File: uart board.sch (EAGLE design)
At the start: 15 parts, among them IC2 74LS688N, IC3 74LS590N

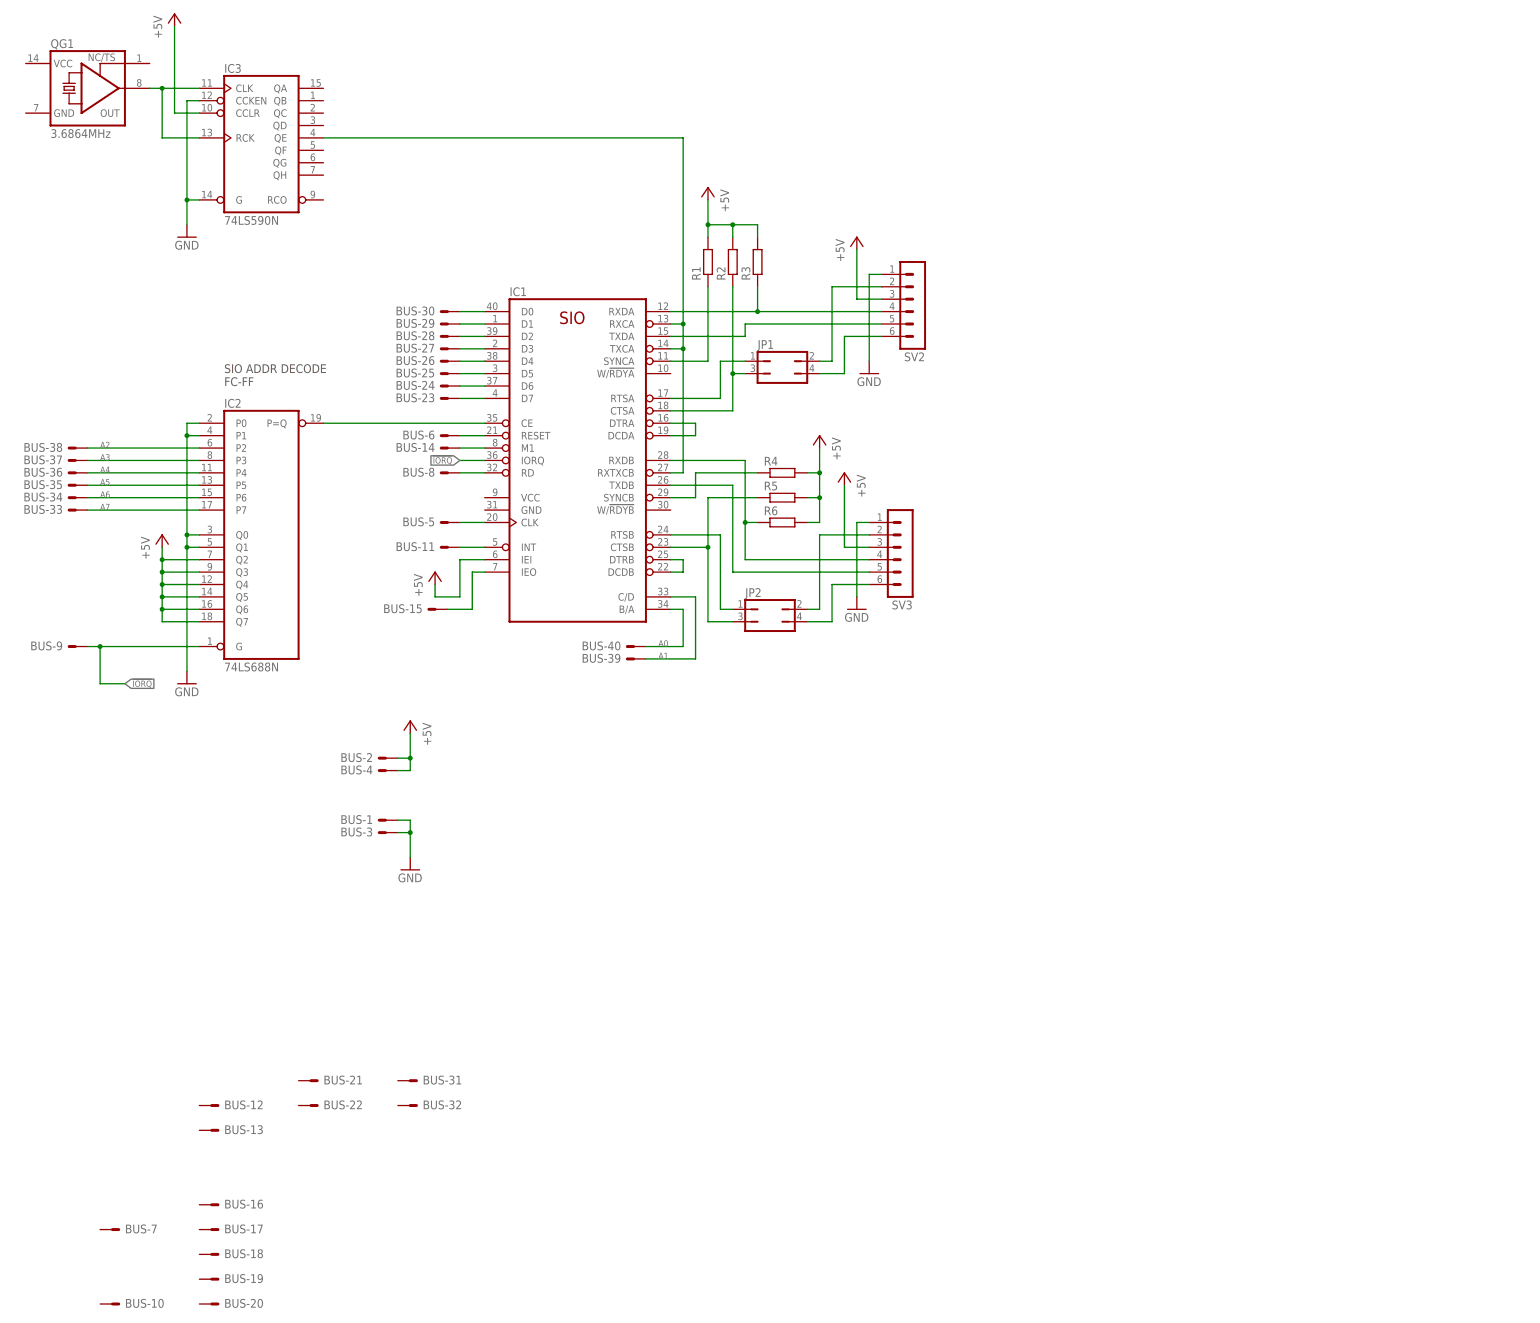
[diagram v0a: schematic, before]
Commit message: Interrupt daisy chain modification
To overcome the issue identified earlier, it seems better to change the interrupt daisy chain to make the CTC the higher priority device. This also simplifies the extra required circuitry to only a single OR gate (U13A).

Now, only when the IEO/ signal of the CTC is asserted will the board drive the data bus to the CPU.

Also added in a previous revision is changes to the beeper circuit. Will now be driven by a 555 timer, gated by the output register.
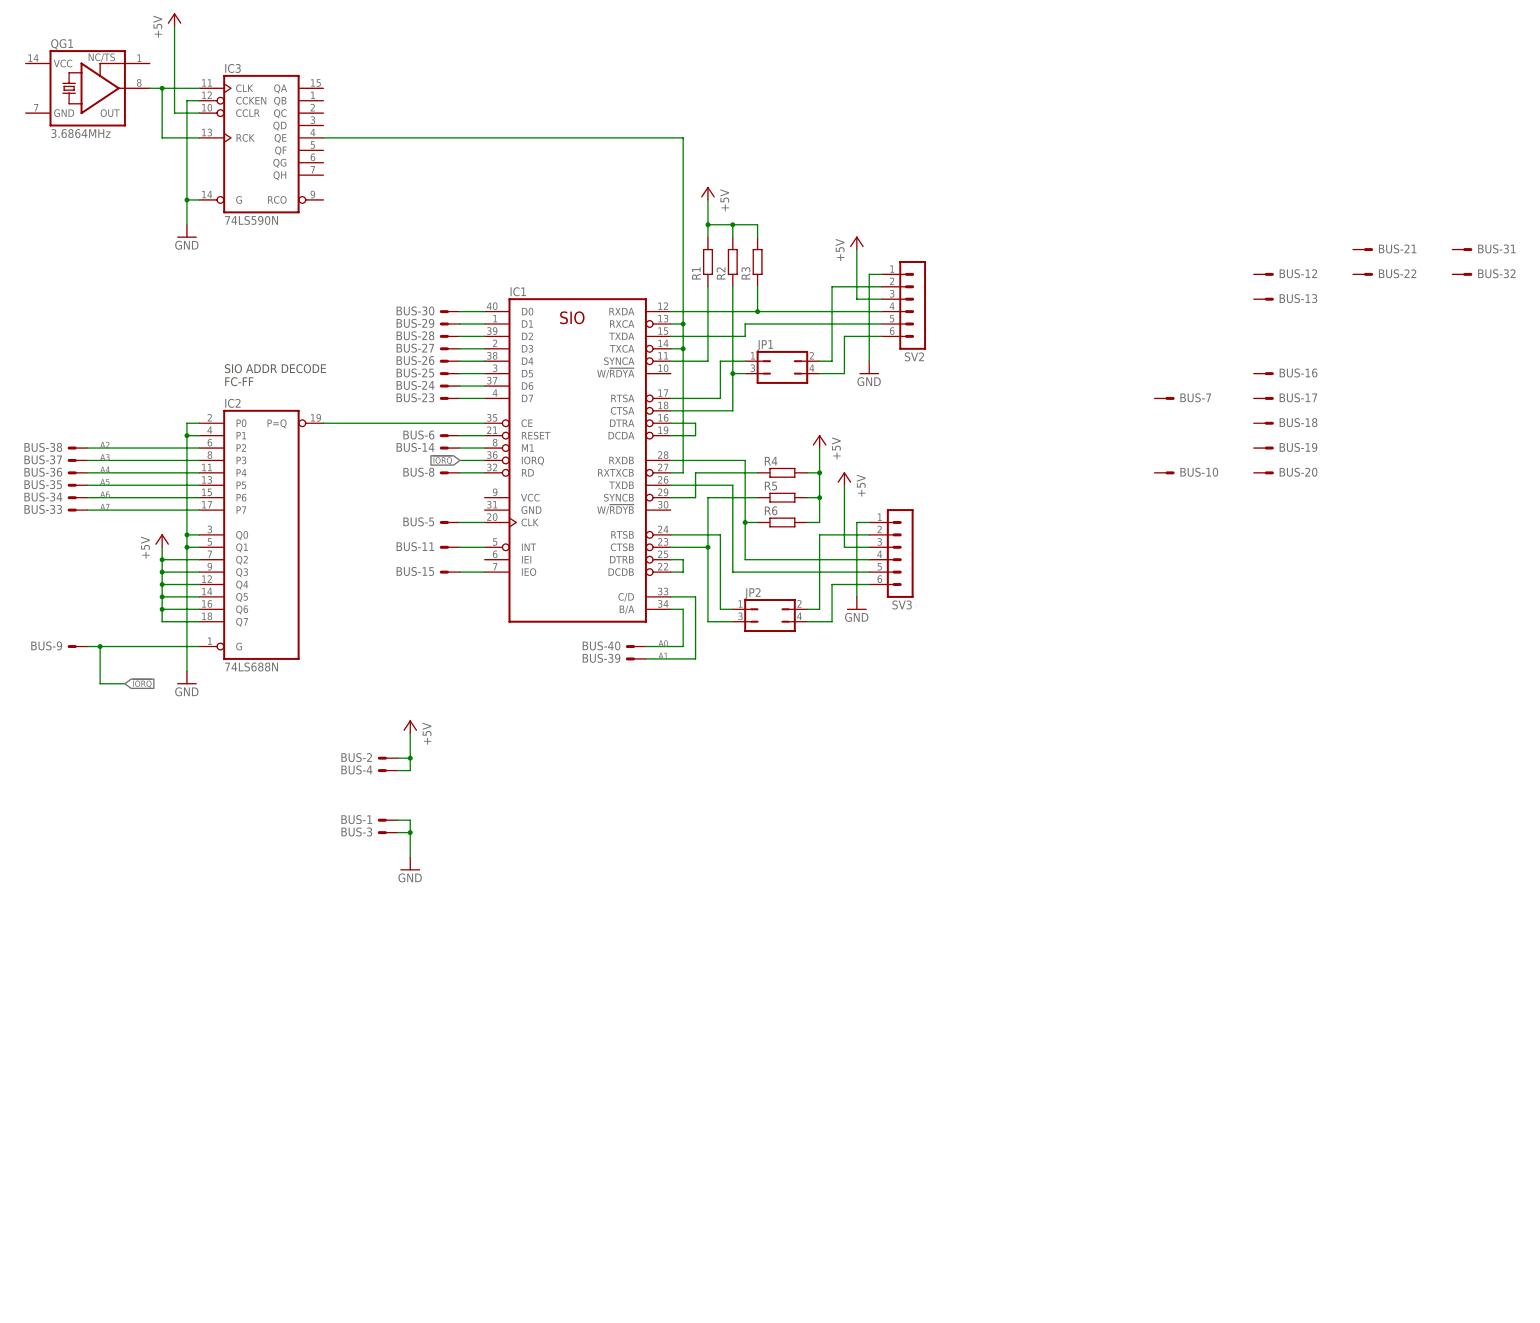
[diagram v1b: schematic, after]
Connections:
- net +5V: no longer IC1.IEI
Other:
- moved on the sheet: BUS-10, BUS-12, BUS-13, BUS-15, BUS-16, BUS-17, BUS-18, BUS-19, BUS-20, BUS-21, BUS-22, BUS-31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
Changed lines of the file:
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@@
 <part name="P+7" library="supply1" deviceset="+5V" device=""/>
 <part name="GND5" library="supply1" deviceset="GND" device=""/>
-<part name="P+8" library="supply1" deviceset="+5V" device=""/>
 </parts>
 <sheets>
@@
 <attribute name="VALUE" x="109.474" y="93.599" size="1.778" layer="96" rot="MR0"/>
 </instance>
-<instance part="BUS" gate="-7" x="40.64" y="-66.04" smashed="yes">
-<attribute name="NAME" x="43.18" y="-66.802" size="1.778" layer="95"/>
-<attribute name="VALUE" x="40.386" y="-68.961" size="1.778" layer="96"/>
+<instance part="BUS" gate="-7" x="256.54" y="104.14" smashed="yes">
+<attribute name="NAME" x="259.08" y="103.378" size="1.778" layer="95"/>
+<attribute name="VALUE" x="256.286" y="101.219" size="1.778" layer="96"/>
 </instance>
 <instance part="BUS" gate="-8" x="109.22" y="88.9" smashed="yes" rot="MR0">
@@
 <attribute name="VALUE" x="33.274" y="50.419" size="1.778" layer="96" rot="MR0"/>
 </instance>
-<instance part="BUS" gate="-10" x="40.64" y="-81.28" smashed="yes">
-<attribute name="NAME" x="43.18" y="-82.042" size="1.778" layer="95"/>
-<attribute name="VALUE" x="40.386" y="-84.201" size="1.778" layer="96"/>
+<instance part="BUS" gate="-10" x="256.54" y="88.9" smashed="yes">
+<attribute name="NAME" x="259.08" y="88.138" size="1.778" layer="95"/>
+<attribute name="VALUE" x="256.286" y="85.979" size="1.778" layer="96"/>
 </instance>
 <instance part="BUS" gate="-11" x="109.22" y="73.66" smashed="yes" rot="MR0">
@@
 <attribute name="VALUE" x="109.474" y="70.739" size="1.778" layer="96" rot="MR0"/>
 </instance>
-<instance part="BUS" gate="-12" x="60.96" y="-40.64" smashed="yes">
-<attribute name="NAME" x="63.5" y="-41.402" size="1.778" layer="95"/>
-<attribute name="VALUE" x="60.706" y="-43.561" size="1.778" layer="96"/>
-</instance>
-<instance part="BUS" gate="-13" x="60.96" y="-45.72" smashed="yes">
-<attribute name="NAME" x="63.5" y="-46.482" size="1.778" layer="95"/>
-<attribute name="VALUE" x="60.706" y="-48.641" size="1.778" layer="96"/>
+<instance part="BUS" gate="-12" x="276.86" y="129.54" smashed="yes">
+<attribute name="NAME" x="279.4" y="128.778" size="1.778" layer="95"/>
+<attribute name="VALUE" x="276.606" y="126.619" size="1.778" layer="96"/>
+</instance>
+<instance part="BUS" gate="-13" x="276.86" y="124.46" smashed="yes">
+<attribute name="NAME" x="279.4" y="123.698" size="1.778" layer="95"/>
+<attribute name="VALUE" x="276.606" y="121.539" size="1.778" layer="96"/>
 </instance>
 <instance part="BUS" gate="-14" x="109.22" y="93.98" smashed="yes" rot="MR0">
@@
 <attribute name="VALUE" x="109.474" y="91.059" size="1.778" layer="96" rot="MR0"/>
 </instance>
-<instance part="BUS" gate="-15" x="106.68" y="60.96" smashed="yes" rot="MR0">
-<attribute name="NAME" x="104.14" y="60.198" size="1.778" layer="95" rot="MR0"/>
-<attribute name="VALUE" x="106.934" y="58.039" size="1.778" layer="96" rot="MR0"/>
-</instance>
-<instance part="BUS" gate="-16" x="60.96" y="-60.96" smashed="yes">
-<attribute name="NAME" x="63.5" y="-61.722" size="1.778" layer="95"/>
-<attribute name="VALUE" x="60.706" y="-63.881" size="1.778" layer="96"/>
-</instance>
-<instance part="BUS" gate="-17" x="60.96" y="-66.04" smashed="yes">
-<attribute name="NAME" x="63.5" y="-66.802" size="1.778" layer="95"/>
-<attribute name="VALUE" x="60.706" y="-68.961" size="1.778" layer="96"/>
-</instance>
-<instance part="BUS" gate="-18" x="60.96" y="-71.12" smashed="yes">
-<attribute name="NAME" x="63.5" y="-71.882" size="1.778" layer="95"/>
-<attribute name="VALUE" x="60.706" y="-74.041" size="1.778" layer="96"/>
-</instance>
-<instance part="BUS" gate="-19" x="60.96" y="-76.2" smashed="yes">
-<attribute name="NAME" x="63.5" y="-76.962" size="1.778" layer="95"/>
-<attribute name="VALUE" x="60.706" y="-79.121" size="1.778" layer="96"/>
-</instance>
-<instance part="BUS" gate="-20" x="60.96" y="-81.28" smashed="yes">
-<attribute name="NAME" x="63.5" y="-82.042" size="1.778" layer="95"/>
-<attribute name="VALUE" x="60.706" y="-84.201" size="1.778" layer="96"/>
-</instance>
-<instance part="BUS" gate="-21" x="81.28" y="-35.56" smashed="yes">
-<attribute name="NAME" x="83.82" y="-36.322" size="1.778" layer="95"/>
-<attribute name="VALUE" x="81.026" y="-38.481" size="1.778" layer="96"/>
-</instance>
-<instance part="BUS" gate="-22" x="81.28" y="-40.64" smashed="yes">
-<attribute name="NAME" x="83.82" y="-41.402" size="1.778" layer="95"/>
-<attribute name="VALUE" x="81.026" y="-43.561" size="1.778" layer="96"/>
+<instance part="BUS" gate="-15" x="109.22" y="68.58" smashed="yes" rot="MR0">
+<attribute name="NAME" x="106.68" y="67.818" size="1.778" layer="95" rot="MR0"/>
+<attribute name="VALUE" x="109.474" y="65.659" size="1.778" layer="96" rot="MR0"/>
+</instance>
+<instance part="BUS" gate="-16" x="276.86" y="109.22" smashed="yes">
+<attribute name="NAME" x="279.4" y="108.458" size="1.778" layer="95"/>
+<attribute name="VALUE" x="276.606" y="106.299" size="1.778" layer="96"/>
+</instance>
+<instance part="BUS" gate="-17" x="276.86" y="104.14" smashed="yes">
+<attribute name="NAME" x="279.4" y="103.378" size="1.778" layer="95"/>
+<attribute name="VALUE" x="276.606" y="101.219" size="1.778" layer="96"/>
+</instance>
+<instance part="BUS" gate="-18" x="276.86" y="99.06" smashed="yes">
+<attribute name="NAME" x="279.4" y="98.298" size="1.778" layer="95"/>
+<attribute name="VALUE" x="276.606" y="96.139" size="1.778" layer="96"/>
+</instance>
+<instance part="BUS" gate="-19" x="276.86" y="93.98" smashed="yes">
+<attribute name="NAME" x="279.4" y="93.218" size="1.778" layer="95"/>
+<attribute name="VALUE" x="276.606" y="91.059" size="1.778" layer="96"/>
+</instance>
+<instance part="BUS" gate="-20" x="276.86" y="88.9" smashed="yes">
+<attribute name="NAME" x="279.4" y="88.138" size="1.778" layer="95"/>
+<attribute name="VALUE" x="276.606" y="85.979" size="1.778" layer="96"/>
+</instance>
+<instance part="BUS" gate="-21" x="297.18" y="134.62" smashed="yes">
+<attribute name="NAME" x="299.72" y="133.858" size="1.778" layer="95"/>
+<attribute name="VALUE" x="296.926" y="131.699" size="1.778" layer="96"/>
+</instance>
+<instance part="BUS" gate="-22" x="297.18" y="129.54" smashed="yes">
+<attribute name="NAME" x="299.72" y="128.778" size="1.778" layer="95"/>
+<attribute name="VALUE" x="296.926" y="126.619" size="1.778" layer="96"/>
 </instance>
 <instance part="BUS" gate="-23" x="109.22" y="104.14" smashed="yes" rot="MR0">
@@
 <attribute name="VALUE" x="109.474" y="118.999" size="1.778" layer="96" rot="MR0"/>
 </instance>
-<instance part="BUS" gate="-31" x="101.6" y="-35.56" smashed="yes">
-<attribute name="NAME" x="104.14" y="-36.322" size="1.778" layer="95"/>
-<attribute name="VALUE" x="101.346" y="-38.481" size="1.778" layer="96"/>
-</instance>
-<instance part="BUS" gate="-32" x="101.6" y="-40.64" smashed="yes">
-<attribute name="NAME" x="104.14" y="-41.402" size="1.778" layer="95"/>
-<attribute name="VALUE" x="101.346" y="-43.561" size="1.778" layer="96"/>
+<instance part="BUS" gate="-31" x="317.5" y="134.62" smashed="yes">
+<attribute name="NAME" x="320.04" y="133.858" size="1.778" layer="95"/>
+<attribute name="VALUE" x="317.246" y="131.699" size="1.778" layer="96"/>
+</instance>
+<instance part="BUS" gate="-32" x="317.5" y="129.54" smashed="yes">
+<attribute name="NAME" x="320.04" y="128.778" size="1.778" layer="95"/>
+<attribute name="VALUE" x="317.246" y="126.619" size="1.778" layer="96"/>
 </instance>
 <instance part="BUS" gate="-33" x="33.02" y="81.28" smashed="yes" rot="MR0">
@@
 <instance part="GND5" gate="1" x="101.6" y="7.62" smashed="yes">
 <attribute name="VALUE" x="99.06" y="5.08" size="1.778" layer="96"/>
-</instance>
-<instance part="P+8" gate="1" x="106.68" y="68.58" smashed="yes">
-<attribute name="VALUE" x="104.14" y="63.5" size="1.778" layer="96" rot="R90"/>
 </instance>
 </instances>
@@
 <junction x="101.6" y="30.48"/>
 </segment>
-<segment>
-<pinref part="IC1" gate="1" pin="IEI"/>
-<wire x1="116.84" y1="71.12" x2="111.76" y2="71.12" width="0.1524" layer="91"/>
-<wire x1="111.76" y1="71.12" x2="111.76" y2="63.5" width="0.1524" layer="91"/>
-<pinref part="P+8" gate="1" pin="+5V"/>
-<wire x1="111.76" y1="63.5" x2="106.68" y2="63.5" width="0.1524" layer="91"/>
-<wire x1="106.68" y1="63.5" x2="106.68" y2="66.04" width="0.1524" layer="91"/>
-</segment>
 </net>
 <net name="N$2" class="0">
@@
 <segment>
 <pinref part="IC1" gate="1" pin="IEO"/>
-<wire x1="116.84" y1="68.58" x2="114.3" y2="68.58" width="0.1524" layer="91"/>
-<wire x1="114.3" y1="68.58" x2="114.3" y2="60.96" width="0.1524" layer="91"/>
-<wire x1="114.3" y1="60.96" x2="109.22" y2="60.96" width="0.1524" layer="91"/>
+<wire x1="116.84" y1="68.58" x2="111.76" y2="68.58" width="0.1524" layer="91"/>
 <pinref part="BUS" gate="-15" pin="S"/>
 </segment>

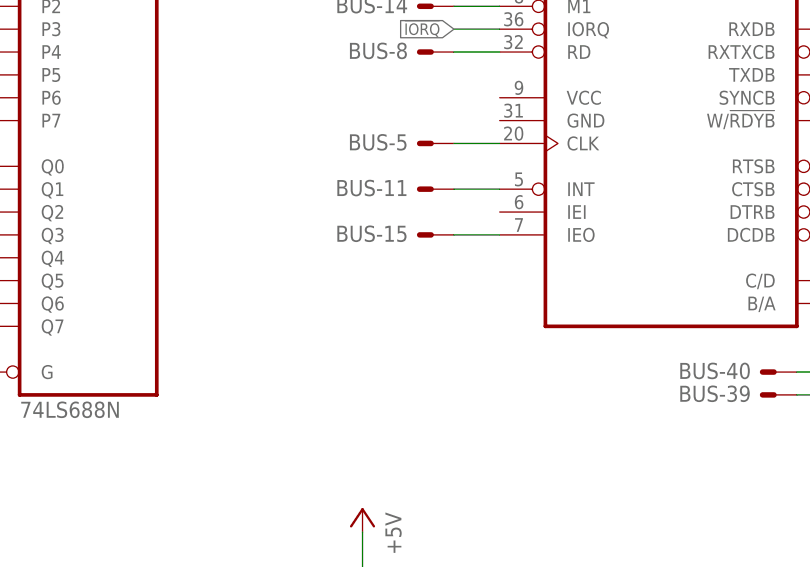
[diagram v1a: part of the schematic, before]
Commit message: Correct schematic for new interrupt daisy chain priority
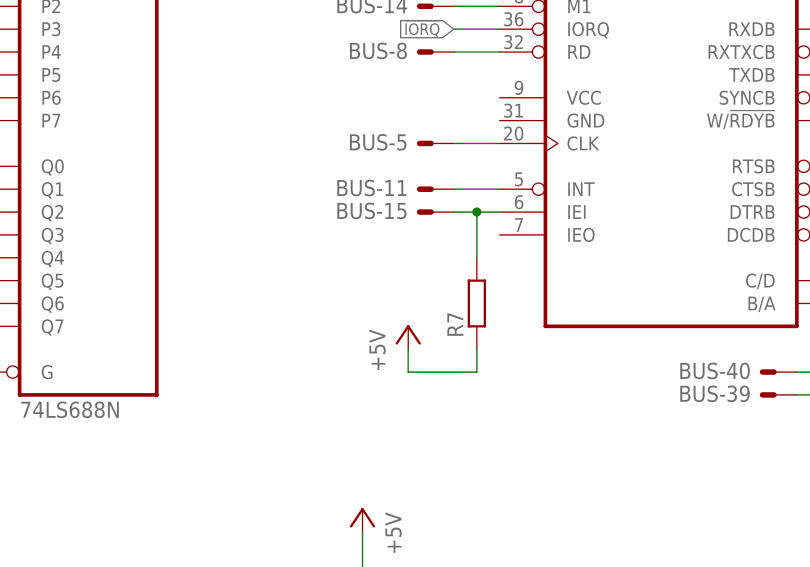
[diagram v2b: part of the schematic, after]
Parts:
- added R7: (no value), rcl:R-EU_0207/10
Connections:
- removed net N$28: BUS-15.S, IC1.IEO
- new net N$27: BUS-15.S, IC1.IEI, R7.2
- net +5V: now also R7.1
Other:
- moved on the sheet: BUS-15
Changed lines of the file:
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@@
 <part name="P+7" library="supply1" deviceset="+5V" device=""/>
 <part name="GND5" library="supply1" deviceset="GND" device=""/>
+<part name="R7" library="rcl" deviceset="R-EU_" device="0207/10"/>
+<part name="P+8" library="supply1" deviceset="+5V" device=""/>
 </parts>
 <sheets>
@@
 <attribute name="VALUE" x="109.474" y="91.059" size="1.778" layer="96" rot="MR0"/>
 </instance>
-<instance part="BUS" gate="-15" x="109.22" y="68.58" smashed="yes" rot="MR0">
-<attribute name="NAME" x="106.68" y="67.818" size="1.778" layer="95" rot="MR0"/>
-<attribute name="VALUE" x="109.474" y="65.659" size="1.778" layer="96" rot="MR0"/>
+<instance part="BUS" gate="-15" x="109.22" y="71.12" smashed="yes" rot="MR0">
+<attribute name="NAME" x="106.68" y="70.358" size="1.778" layer="95" rot="MR0"/>
+<attribute name="VALUE" x="109.474" y="68.199" size="1.778" layer="96" rot="MR0"/>
 </instance>
 <instance part="BUS" gate="-16" x="276.86" y="109.22" smashed="yes">
@@
 <instance part="GND5" gate="1" x="101.6" y="7.62" smashed="yes">
 <attribute name="VALUE" x="99.06" y="5.08" size="1.778" layer="96"/>
+</instance>
+<instance part="R7" gate="G$1" x="114.3" y="60.96" smashed="yes" rot="R90">
+<attribute name="NAME" x="112.8014" y="57.15" size="1.778" layer="95" rot="R90"/>
+<attribute name="VALUE" x="117.602" y="57.15" size="1.778" layer="96" rot="R90"/>
+</instance>
+<instance part="P+8" gate="1" x="106.68" y="58.42" smashed="yes">
+<attribute name="VALUE" x="104.14" y="53.34" size="1.778" layer="96" rot="R90"/>
 </instance>
 </instances>
@@
 <junction x="101.6" y="30.48"/>
 </segment>
+<segment>
+<pinref part="P+8" gate="1" pin="+5V"/>
+<wire x1="106.68" y1="55.88" x2="106.68" y2="53.34" width="0.1524" layer="91"/>
+<wire x1="106.68" y1="53.34" x2="114.3" y2="53.34" width="0.1524" layer="91"/>
+<pinref part="R7" gate="G$1" pin="1"/>
+<wire x1="114.3" y1="53.34" x2="114.3" y2="55.88" width="0.1524" layer="91"/>
+</segment>
 </net>
 <net name="N$2" class="0">
@@
 </segment>
 </net>
-<net name="N$28" class="0">
-<segment>
-<pinref part="IC1" gate="1" pin="IEO"/>
-<wire x1="116.84" y1="68.58" x2="111.76" y2="68.58" width="0.1524" layer="91"/>
+<net name="N$27" class="0">
+<segment>
 <pinref part="BUS" gate="-15" pin="S"/>
-</segment>
-</net>
+<pinref part="IC1" gate="1" pin="IEI"/>
+<wire x1="111.76" y1="71.12" x2="114.3" y2="71.12" width="0.1524" layer="91"/>
+<pinref part="R7" gate="G$1" pin="2"/>
+<wire x1="114.3" y1="71.12" x2="116.84" y2="71.12" width="0.1524" layer="91"/>
+<wire x1="114.3" y1="66.04" x2="114.3" y2="71.12" width="0.1524" layer="91"/>
+<junction x="114.3" y="71.12"/>
+</segment>
+</net>
